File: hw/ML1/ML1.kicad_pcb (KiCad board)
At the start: 2 copper layers, 111 x 63 mm, 64 parts, among them J1 Conn_01x06, J2 5-12V Supply, J3 Conn_01x20, J4 Conn_01x02, T1 Transformer_1P_1S, T2 Transformer_1P_1S, U1 LMV324 (Actually LTV9161), U2 LTV-356T, U3 NCP1117-3.3_SOT223, U4 MCP4725xxx-xCH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

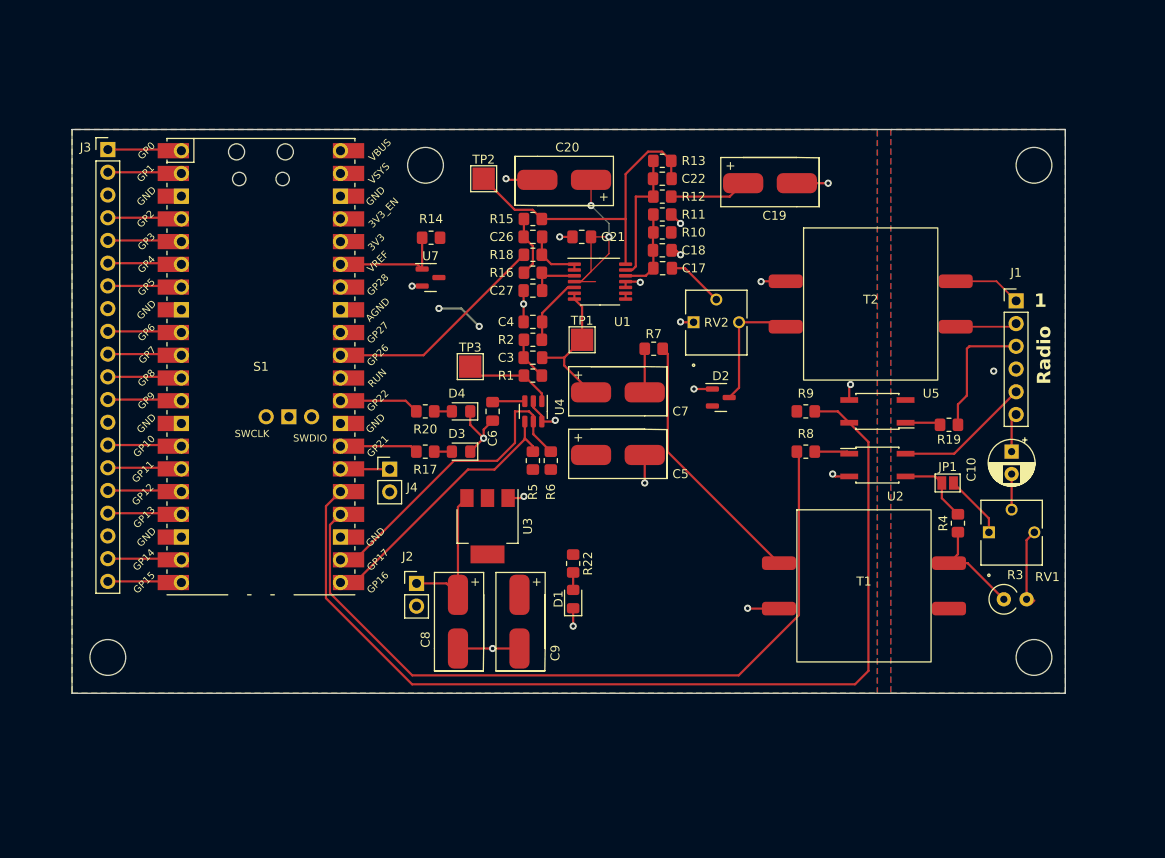
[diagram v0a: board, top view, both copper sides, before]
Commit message: Re-work of ML1 board in process
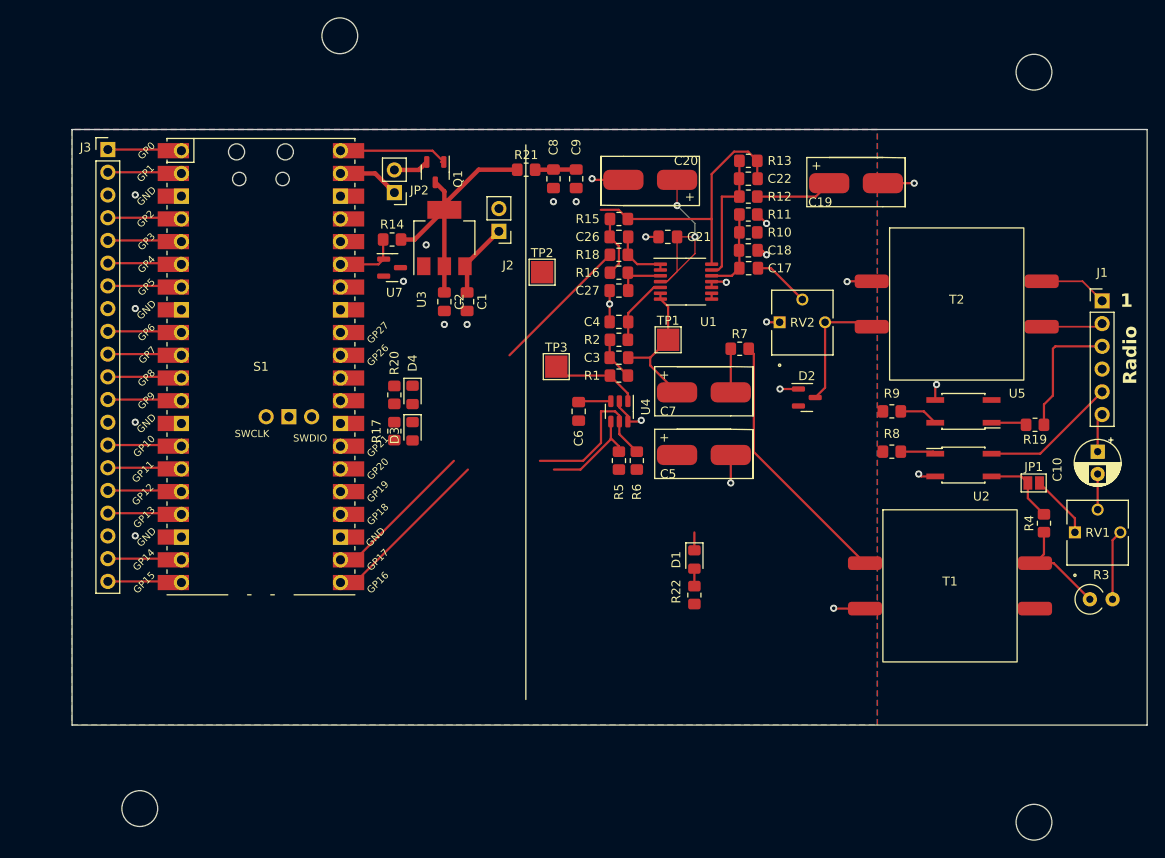
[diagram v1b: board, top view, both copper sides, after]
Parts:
- removed J4: Conn_01x02, Connector_PinHeader_2.54mm:PinHeader_1x02_P2.54mm_Vertical
- added C1: 10u, Capacitor_SMD:C_0805_2012Metric_Pad1.18x1.45mm_HandSolder, F.Cu at (168.1, 63.2)
- added C2: 10u, Capacitor_SMD:C_0805_2012Metric_Pad1.18x1.45mm_HandSolder, F.Cu at (165.6, 63.2)
- added JP2: Jumper_2_Bridged, Connector_PinHeader_2.54mm:PinHeader_1x02_P2.54mm_Vertical, F.Cu at (160.0, 51.1)
- added Q1: DMG2305UX-13, Package_TO_SOT_SMD:SOT-23-3, F.Cu at (164.6, 48.8)
- added R21: 47, Resistor_SMD:R_0805_2012Metric_Pad1.20x1.40mm_HandSolder, F.Cu at (174.8, 48.5)
- C19, C20, C5, C7: footprint KiCad-Library:CAP_KEMET_530_530 -> bruce-footprints:CAP_KEMET_530_530
- C8, C9: value 10u -> 47u; footprint KiCad-Library:CAP_KEMET_530_530 -> Capacitor_SMD:C_0805_2012Metric_Pad1.18x1.45mm_HandSolder
- RV1, RV2: footprint KiCad-Library:POT_3362P -> bruce-footprints:POT_3362P
- S1: footprint KiCad-Library:RPi_PicoW_SMD_TH -> bruce-footprints:RPi_PicoW_SMD_TH
- T1, T2: footprint KiCad-Library:CheapAudioTransformer -> bruce-footprints:CheapAudioTransformer
- moved C8 50.7 mm to (177.8, 49.5)
- moved C9 49.9 mm to (180.3, 49.5)
- moved J2 40.4 mm to (171.7, 55.4), turned to 180 degrees
- moved U3 32.6 mm to (165.6, 56.1), turned to 90 degrees
- moved H1 18.4 mm to (231.5, 121.4)
- moved H3 17.4 mm to (153.9, 33.5)
- moved H4 17.3 mm to (131.6, 119.9)
- moved D1 14.3 mm to (193.5, 92.1), turned to -90 degrees
- moved R22 14.0 mm to (193.5, 96.0), turned to 90 degrees
- moved TP2 12.3 mm to (176.5, 59.9)
- moved H2 10.4 mm to (231.5, 37.6)
- moved C10 9.61 mm to (238.6, 80.0)
- moved C17 9.61 mm to (199.6, 59.5)
- moved C18 9.61 mm to (199.6, 57.5)
- moved C19 9.61 mm to (211.6, 50.1)
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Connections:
- C8 pad 1: +5VA -> +3.3VA
- R14 pad 1: +3.3VA -> +3.3V
- R22 pad 1: +3.3VA -> +3.3V
- S1 pad 26: GPIO_PWR -> unconnected-(S1-GP20-Pad26)
- U3 pad 2: +3.3VA -> +3.3V
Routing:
- net GPIO_COS: track 110.8 -> 4.38 mm
- net GPIO_PTT: track 86.6 -> 0.00 mm
- net +3.3V: track 0.00 -> 29.3 mm
- net GNDA: track 57.9 -> 39.9 mm, vias 20 -> 25
- net Net-(Q1-G): track 0.00 -> 12.4 mm
- net ADC0: track 25.2 -> 15.9 mm
- net LED1: track 8.97 -> 0.00 mm
- net LED0: track 8.73 -> 0.00 mm
- net +5VA: track 16.4 -> 8.72 mm
- net Net-(JP2-A): track 0.00 -> 6.91 mm
- net Net-(S1-ADC_VREF): track 12.8 -> 7.29 mm
- net GPIO_PWR: track 5.51 -> 0.00 mm
- net Net-(C22-Pad2): track 36.4 -> 31.5 mm
- net Net-(JP2-B): track 0.00 -> 3.99 mm
- net +3.3VA: track 33.0 -> 29.9 mm, vias 4 -> 2
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- added copper zone on F.Cu, net GNDA
- removed copper zone on F.Cu, net +3.3VA
- removed copper zone on B.Cu, net RIG_GND
- removed copper zone on F.Cu, net RIG_GND
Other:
- board size 111 x 63 mm -> 120.1 x 66.6 mm

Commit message: Re-work of ML1 board in process
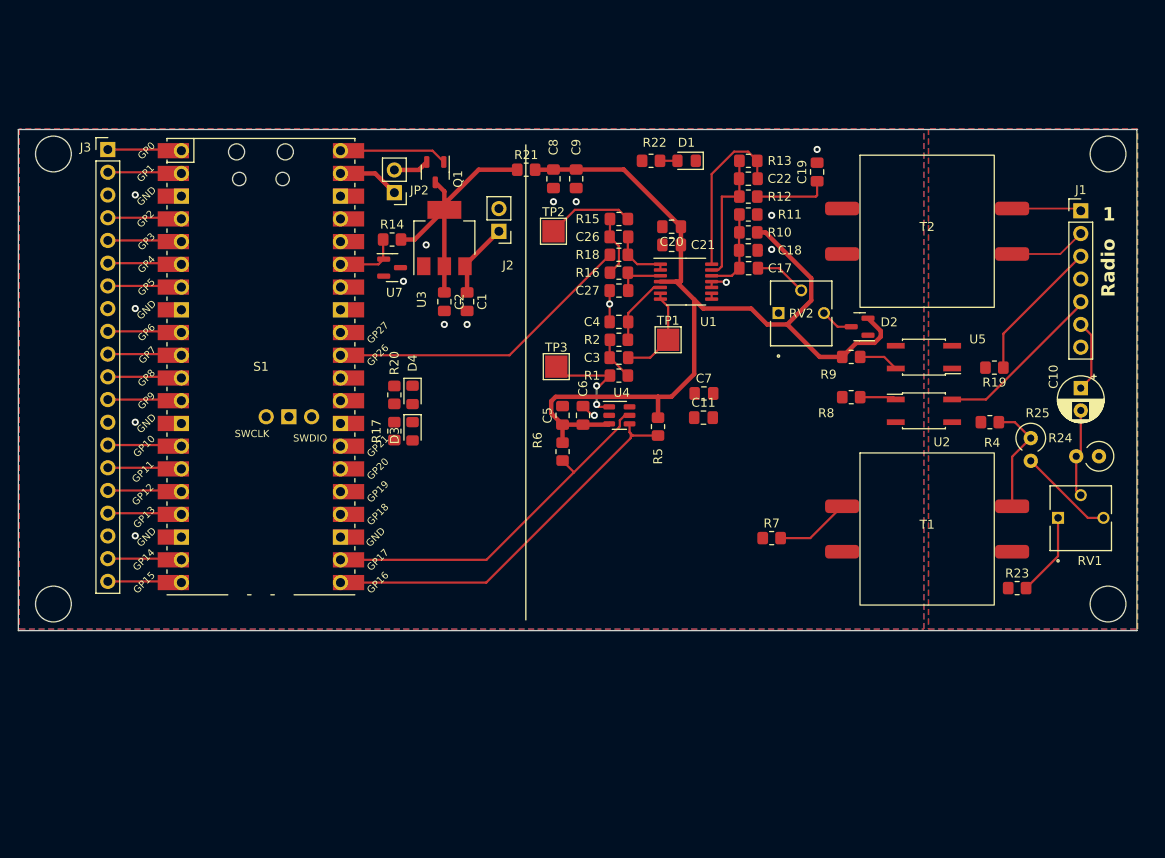
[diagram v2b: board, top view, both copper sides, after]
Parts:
- removed JP1: SolderJumper_2_Open, Jumper:SolderJumper-2_P1.3mm_Open_Pad1.0x1.5mm
- removed R3: 10k, Resistor_THT:R_Axial_DIN0309_L9.0mm_D3.2mm_P2.54mm_Vertical
- added C11: 47u, Capacitor_SMD:C_0805_2012Metric_Pad1.18x1.45mm_HandSolder, F.Cu at (194.6, 76.2)
- added R23: 0R, Resistor_SMD:R_0805_2012Metric_Pad1.20x1.40mm_HandSolder, F.Cu at (229.6, 95.2)
- added R24: 1k, Resistor_THT:R_Axial_DIN0309_L9.0mm_D3.2mm_P2.54mm_Vertical, F.Cu at (238.8, 80.5)
- added R25: 33k, Resistor_THT:R_Axial_DIN0309_L9.0mm_D3.2mm_P2.54mm_Vertical, F.Cu at (231.1, 78.5)
- C19: footprint bruce-footprints:CAP_KEMET_530_530 -> Capacitor_SMD:C_0805_2012Metric_Pad1.18x1.45mm_HandSolder
- C20, C7: value 100u -> 47u; footprint bruce-footprints:CAP_KEMET_530_530 -> Capacitor_SMD:C_0805_2012Metric_Pad1.18x1.45mm_HandSolder
- C5: value 10u -> 47u; footprint bruce-footprints:CAP_KEMET_530_530 -> Capacitor_SMD:C_0805_2012Metric_Pad1.18x1.45mm_HandSolder
- J1: value Conn_01x06 -> Conn_01x07; footprint Connector_PinHeader_2.54mm:PinHeader_1x06_P2.54mm_Vertical -> Connector_PinHeader_2.54mm:PinHeader_1x07_P2.54mm_Vertical
- R7: value 1k -> 0R
- moved R22 48.8 mm to (188.7, 47.5), turned to 0 degrees
- moved D1 44.6 mm to (192.7, 47.5), turned to 180 degrees
- moved H3 34.6 mm to (121.9, 46.7)
- moved H1 25.8 mm to (239.8, 97.0)
- moved H4 24.8 mm to (121.9, 97.0)
- moved R7 21.5 mm to (202.2, 89.7)
- moved C5 16.4 mm to (178.8, 75.9), turned to 90 degrees
- moved R4 12.8 mm to (226.6, 76.7), turned to 180 degrees
- moved H2 12.3 mm to (239.8, 46.7)
- moved J1 10.3 mm to (236.7, 53.1)
- moved D2 9.87 mm to (212.0, 66.0), turned to 180 degrees
- moved T2 8.77 mm to (219.6, 55.4)
- moved R6 8.36 mm to (178.8, 80.0), turned to -90 degrees
- moved R19 7.84 mm to (227.1, 70.6)
- moved R8 7.59 mm to (211.1, 73.9)
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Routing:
- net +3.3VA: track 29.9 -> 112.5 mm, vias 2 -> 0
- net GNDA: track 39.9 -> 8.10 mm, vias 25 -> 16
- net Net-(T1-AA): track 29.3 -> 8.35 mm
- net ADC0: track 15.9 -> 34.8 mm
- net I2C0_SDA: track 31.1 -> 43.9 mm
- net Net-(D2-COM): track 14.3 -> 3.68 mm
- net RIG_GND: track 8.60 -> 0.00 mm
- net Net-(C10-Pad2): track 3.98 -> 9.88 mm
- net I2C0_SCL: track 35.5 -> 41.2 mm
- net Net-(U1B--): track 16.0 -> 10.8 mm
- net Net-(C11-Pad2): track 4.87 -> 0.00 mm
- net Net-(R19-Pad2): track 3.95 -> 0.00 mm
- net RIG_PTT: track 15.2 -> 19.1 mm
- net RIG_AF_IN: track 4.36 -> 8.09 mm
- net Net-(C22-Pad2): track 31.5 -> 28.4 mm
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- added copper zone on B.Cu, net RIG_GND
- added copper zone on F.Cu, net RIG_GND
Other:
- board size 120.1 x 66.6 mm -> 125 x 56 mm

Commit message: First draft of board is passing DRC
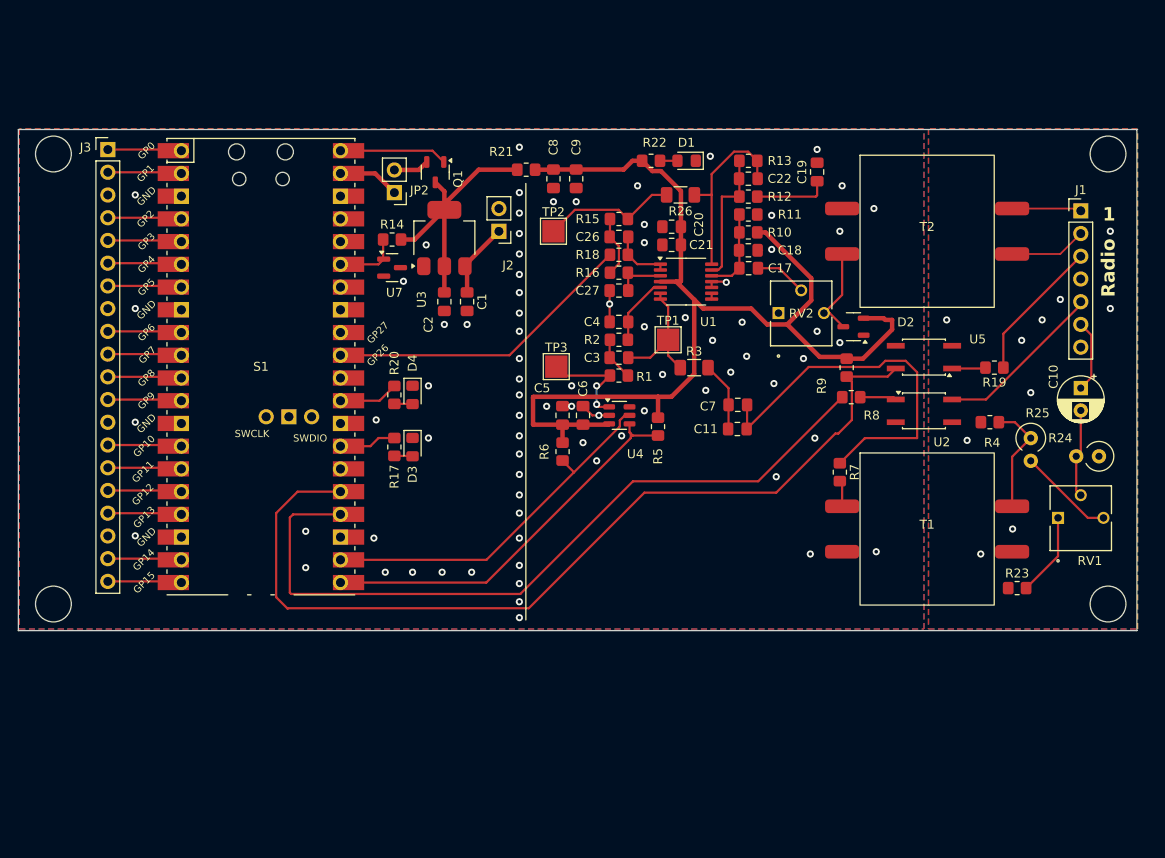
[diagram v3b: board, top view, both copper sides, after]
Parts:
- added R26: 0R, Resistor_SMD:R_1206_3216Metric_Pad1.30x1.75mm_HandSolder, F.Cu at (192.0, 51.3)
- added R3: 0R, Resistor_SMD:R_1206_3216Metric_Pad1.30x1.75mm_HandSolder, F.Cu at (193.5, 70.6)
- D2: footprint Package_TO_SOT_SMD:SOT-23 -> Package_TO_SOT_SMD:SOT-23-3
- moved R7 10.6 mm to (209.8, 82.3), turned to -90 degrees
- moved C11 4.00 mm to (198.4, 77.5)
- moved C7 4.00 mm to (198.4, 74.8)
- moved R17 1.77 mm to (160.0, 79.5)
- moved D3 1.77 mm to (162.1, 79.5)
- moved R9 1.30 mm to (210.6, 70.6), turned to -90 degrees
- moved D2 0.68 mm to (211.3, 66.0)
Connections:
- C11 pad 1: Net-(U1B--) -> Net-(C11-Pad1)
- C7 pad 1: Net-(U1B--) -> Net-(C11-Pad1)
- R15 pad 2: Net-(C22-Pad2) -> Net-(R15-Pad2)
- R22 pad 1: +3.3V -> +3.3VA
- TP2 pad 1: Net-(C22-Pad2) -> Net-(R15-Pad2)
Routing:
- net GPIO_COS: track 4.51 -> 102.1 mm
- net GPIO_PTT: track 0.00 -> 85.1 mm
- net Net-(C11-Pad2): track 0.00 -> 42.6 mm
- net Net-(R15-Pad2): track 0.00 -> 14.7 mm
- net +3.3VA: track 112.5 -> 123.6 mm
- net Net-(C11-Pad1): track 0.00 -> 7.84 mm
- net Net-(C22-Pad2): track 28.4 -> 20.6 mm
- net LED1: track 0.00 -> 6.70 mm
- net Net-(D2-COM): track 3.68 -> 10.2 mm
- net LED0: track 0.00 -> 6.40 mm
- net Net-(T1-AA): track 8.35 -> 2.92 mm
- net Net-(R19-Pad2): track 0.00 -> 3.76 mm
- net Net-(U1B--): track 10.8 -> 14.5 mm
- net GNDA: track 8.10 -> 10.3 mm, vias 16 -> 79
- net Net-(D3-A): track 0.00 -> 2.05 mm
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
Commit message: Final checks, preparing to create GRB
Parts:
- removed R7: 0R, Resistor_SMD:R_0805_2012Metric_Pad1.20x1.40mm_HandSolder
- D2: footprint Package_TO_SOT_SMD:SOT-23-3 -> Package_TO_SOT_SMD:SOT-23
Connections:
- C11 pad 2: Net-(C11-Pad2) -> Net-(T1-AA)
- C7 pad 2: Net-(C11-Pad2) -> Net-(T1-AA)
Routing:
- net Net-(T1-AA): track 2.92 -> 47.3 mm
- net Net-(C11-Pad2): track 42.6 -> 0.00 mm
- net GPIO_COS: track 102.1 -> 86.1 mm, vias 0 -> 2
- net GPIO_PTT: track 85.1 -> 71.9 mm, vias 0 -> 2
- net RIG_GND: vias 10 -> 17
- net GNDA: vias 79 -> 128
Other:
- board text added: "+"
- board text added: "GND"
- board text added: "LED0"
- board text added: "LED1"
- board text added: "MicroLink V1 2024-03 KC1FSZ"
